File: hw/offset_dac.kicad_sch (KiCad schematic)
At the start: 33 parts, among them Q1 SSM6N35AFE, Q3 SSM6N35AFE, U22 TSV992A, U23 MCP47CVB02-E_UN

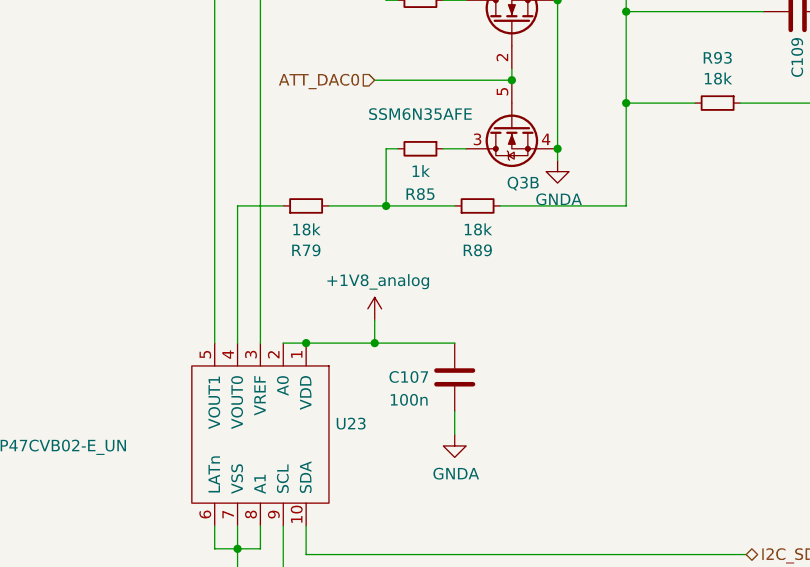
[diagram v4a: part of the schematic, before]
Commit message: rewired 1V8_analog to +2V5_analog
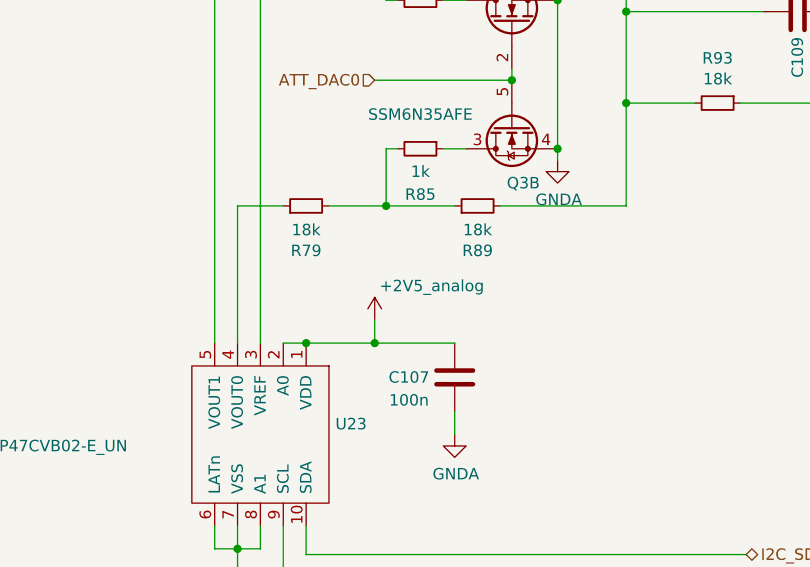
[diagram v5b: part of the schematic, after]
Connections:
- net +1V8_analog is gone; now on net +2V5_analog: C107.2, U23.1 (VDD), U23.2 (A0)
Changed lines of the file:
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@@
-    )
-  )
-  (symbol (lib_id "fmc:+1V8_analog") (at 118.11 139.7 0) (unit 1)
-    (in_bom yes) (on_board yes) (dnp no)
-    (property "Reference" "#PWR075" (at 118.11 143.51 0)
-      (effects (font (size 1.27 1.27)) hide)
-    )
-    (property "Value" "+1V8_analog" (at 118.491 135.3058 0)
-      (effects (font (size 1.27 1.27)))
-    )
-    (property "Footprint" "" (at 118.11 139.7 0)
-      (effects (font (size 1.27 1.27)) hide)
-    )
-    (property "Datasheet" "" (at 118.11 139.7 0)
-      (effects (font (size 1.27 1.27)) hide)
-    )
-    (pin "1")
-    (instances
-      (project "usbadc"
-        (path "/7c8a1f8d-8834-4c9b-aaae-1f231e9b09a1/c969de1a-32a7-4770-b1aa-e527a627ef90/413eeb87-85d0-4a61-9245-920a92a97234"
-          (reference "#PWR075") (unit 1)
-        )
-      )
     )
   )
@@
         )
       )
+    )
+  )
+  (symbol (lib_id "fmc:+2V5_analog") (at 118.11 139.7 0) (unit 1)
+    (in_bom yes) (on_board yes) (dnp no)
+    (property "Reference" "#PWR075" (at 118.11 143.51 0)
+      (effects (font (size 1.27 1.27)) hide)
+    )
+    (property "Value" "+2V5_analog" (at 124.46 135.89 0)
+      (effects (font (size 1.27 1.27)))
+    )
+    (property "Footprint" "" (at 118.11 139.7 0)
+      (effects (font (size 1.27 1.27)) hide)
+    )
+    (property "Datasheet" "" (at 118.11 139.7 0)
+      (effects (font (size 1.27 1.27)) hide)
+    )
+    (pin "1")
+    (instances
+      (project "usbadc"
+        (path "/7c8a1f8d-8834-4c9b-aaae-1f231e9b09a1/c969de1a-32a7-4770-b1aa-e527a627ef90/413eeb87-85d0-4a61-9245-920a92a97234"
+          (reference "#PWR075") (unit 1)
+        )
+      )

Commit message: WIP; converging
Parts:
- added R25, R35: 18k, Resistor_SMD:R_0603_1608Metric, symbol Device:R_Small
- R90, R91: value 9k -> 18k
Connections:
- net GNDA: now also R25.1, R35.1
- net at R86.2, R90.2, U22.3 (+): now also R25.2
- net at R88.2, R91.2, U22.5 (+): now also R35.2
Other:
- moved on the sheet: C108, C109, C110, C111, C112, C113, R92, R93, R94, R95, U22A, U22B

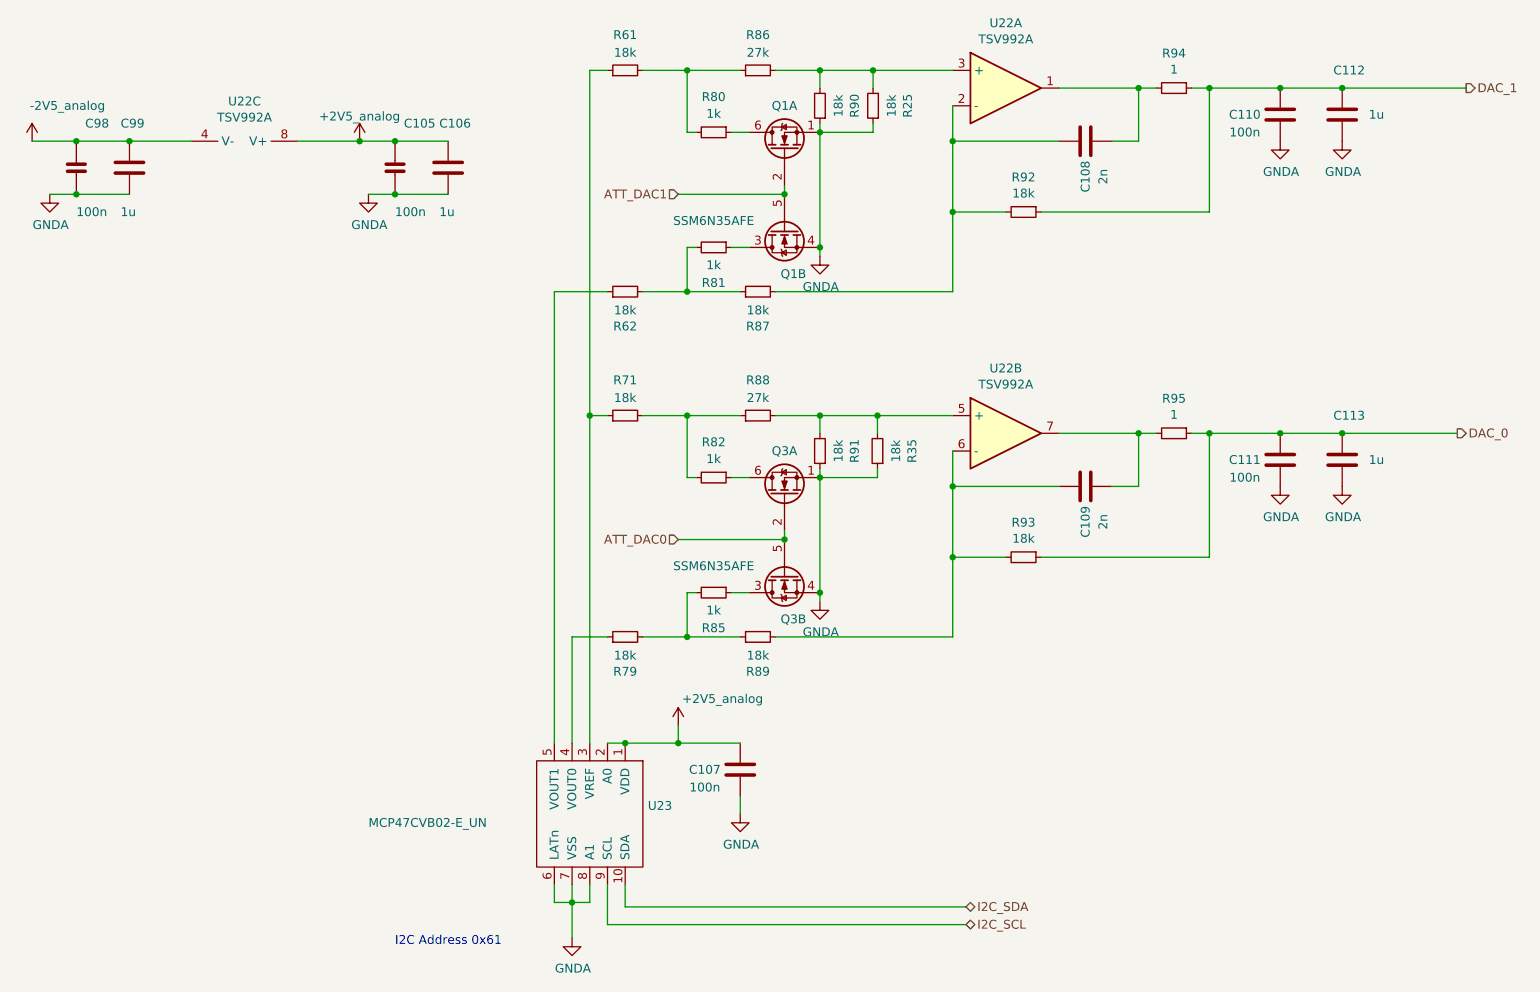
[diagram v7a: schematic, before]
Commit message: consolidated components to simplify BOM
(nothing actually changed but the symbols representing identical
components are now identical -> no more multiple BOM entries for
the same type of component).
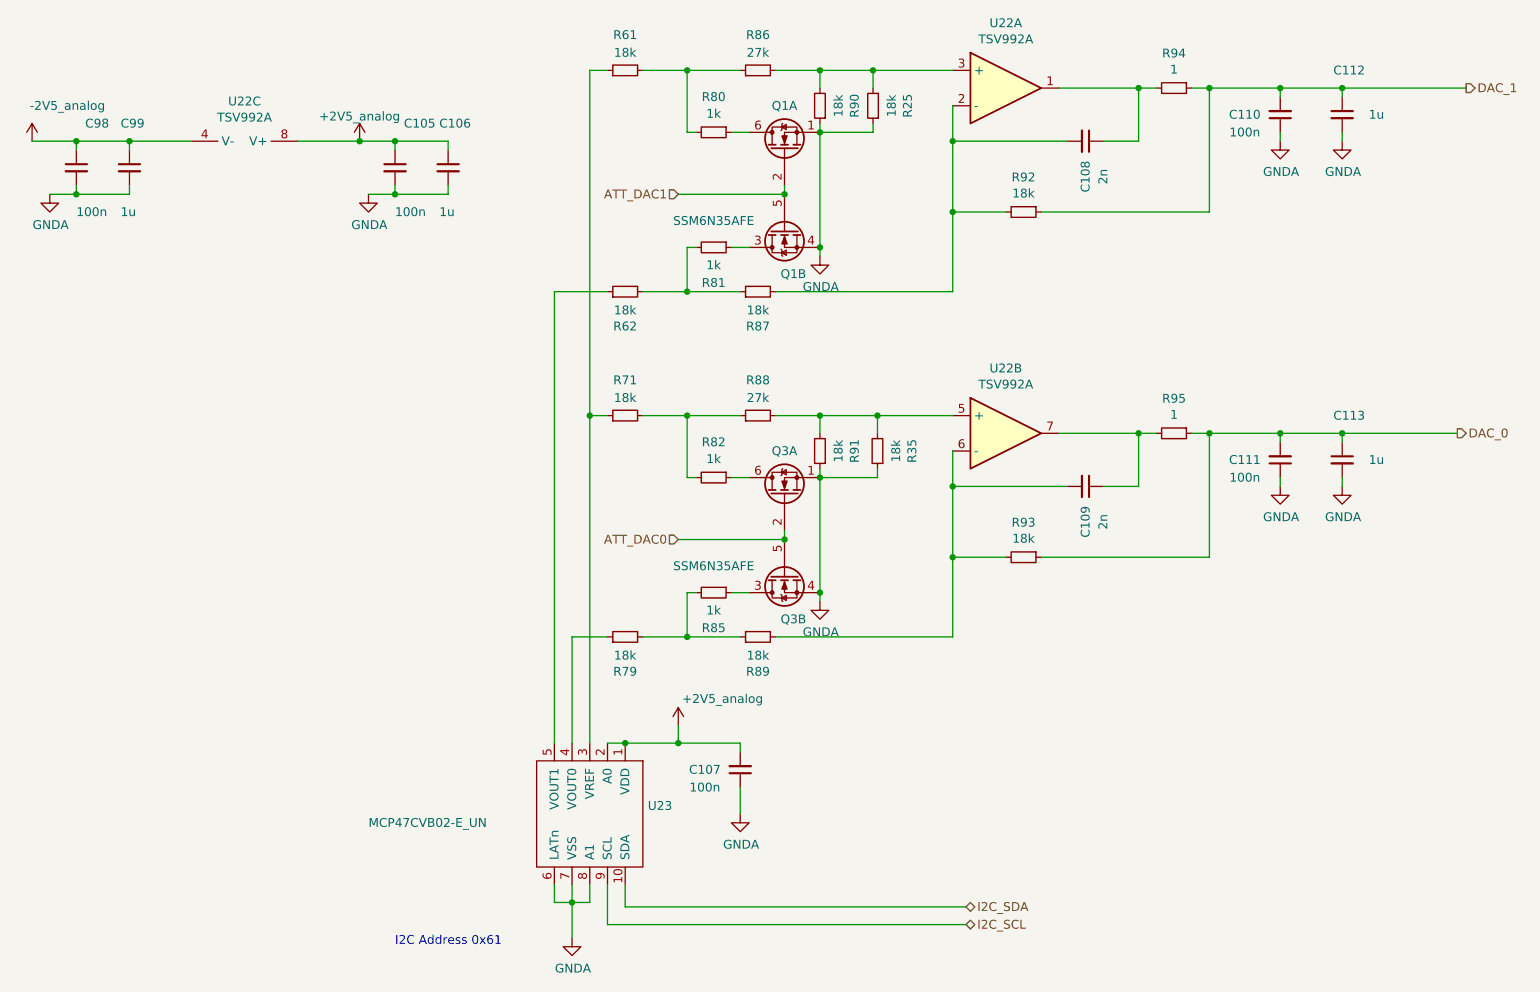
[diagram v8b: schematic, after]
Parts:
- C105, C98: symbol fmc:100nF_402 -> Device:C_Small; Manufacturer (none) -> Samsung; Part (none) -> CL10B104KB8NFN
- C106, C112, C113, C99: symbol fmc:1uF_805 -> Device:C_Small; Manufacturer (none) -> TDK; Part (none) -> CGA4J2X7R1C105K125AA
- C107, C110, C111: symbol fmc:100nF_603 -> Device:C_Small; Manufacturer (none) -> Samsung; Part (none) -> CL10B104KB8NFN
- C108, C109: symbol fmc:100nF_603 -> Device:C_Small
